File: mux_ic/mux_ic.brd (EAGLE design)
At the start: 160 x 100 mm, 12 parts, among them U2 TEXAS_INSTRUMENTS_CD74HC4067M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, U5 TEXAS_INSTRUMENTS_CD74HC4067M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, U6 TEXAS_INSTRUMENTS_CD74HC4067M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, U7 TEXAS_INSTRUMENTS_CD74HC4067M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

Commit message: update
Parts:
- moved U7 21.8 mm to (40.6, 66.0)
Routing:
- net N$22: track 0.00 -> 9.84 mm
- net N$21: track 0.00 -> 6.34 mm

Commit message: update to receive and send
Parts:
- moved JP4 33.3 mm to (64.8, 5.08)
- moved U7 22.9 mm to (40.6, 43.2)
- moved JP5 17.7 mm to (50.8, 5.08)
- moved JP3 16.9 mm to (12.7, 19.1)
- moved JP6 15.5 mm to (36.8, 5.08)
- moved JP8 14.5 mm to (73.7, 20.3), turned to 90 degrees
- moved U6 11.4 mm to (58.4, 43.2)
- moved JP2 10.9 mm to (2.54, 3.81)
- moved JP1 9.67 mm to (15.2, 30.5)
- moved JP7 8.89 mm to (22.9, 5.08)
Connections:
- removed net N$10: JP3.2, U7.1
- net N$4: now also JP3.2; no longer JP2.1
- net N$5: now also JP2.1, U7.1; no longer JP2.2
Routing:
- net N$21: track 6.34 -> 35.9 mm
- net N$22: track 9.84 -> 27.7 mm
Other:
- board size 160 x 100 mm -> 77.5 x 55.5 mm

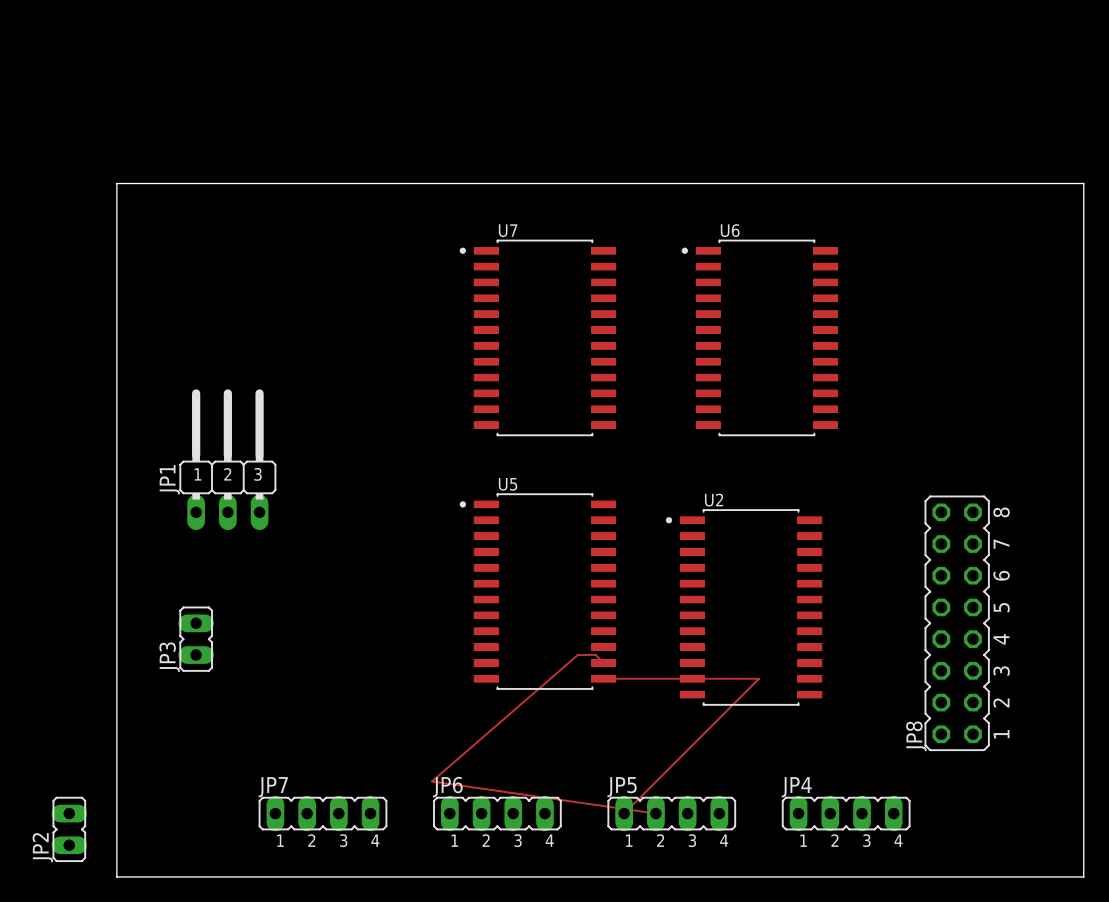
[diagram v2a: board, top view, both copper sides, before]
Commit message: Gentrified board layout and component names
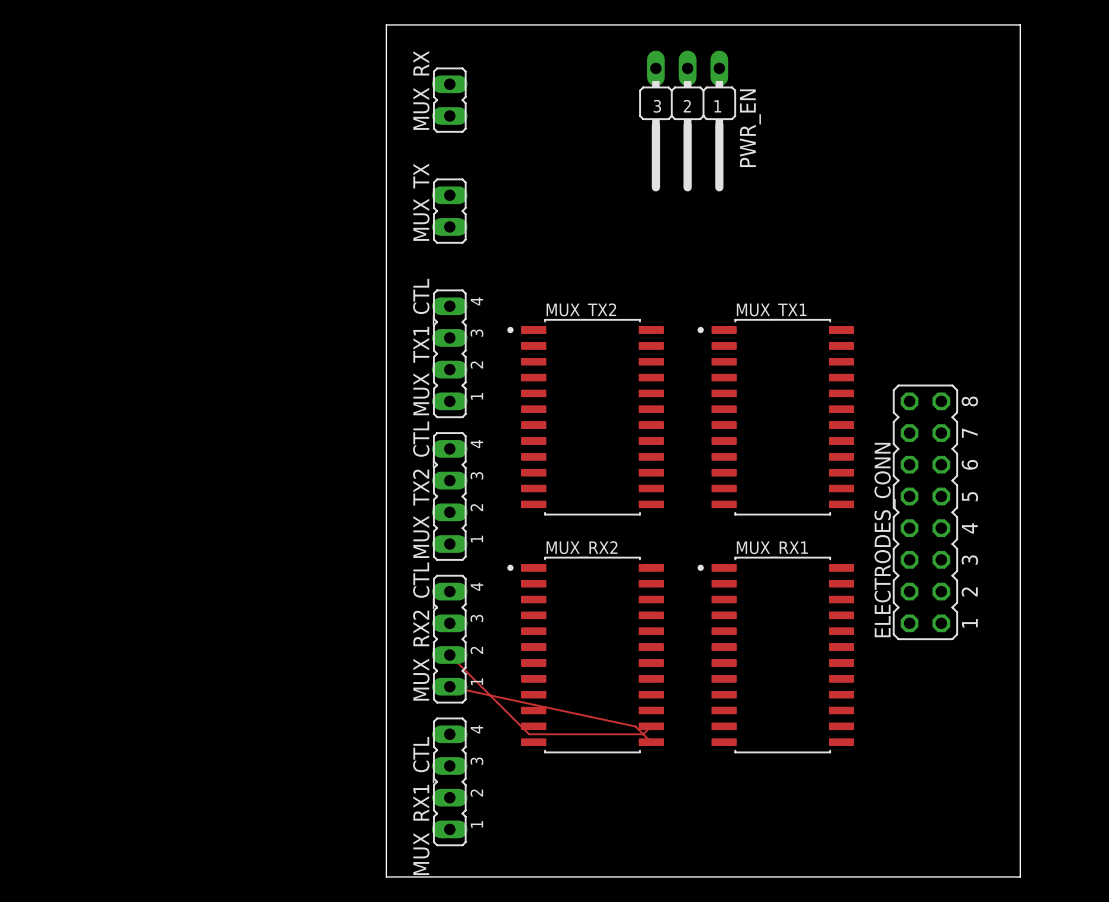
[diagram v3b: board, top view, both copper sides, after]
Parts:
- removed JP1: (no value), jumper:JP2W
- removed JP2, JP3: (no value), jumper:JP1
- removed JP4, JP5, JP6, JP7: (no value), jumper:JP4
- removed JP8: (no value), jumper:JP8Q
- removed U2, U5, U6, U7: TEXAS_INSTRUMENTS_CD74HC4067M96TEXAS_INSTRUMENTS_CD74HC4067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, Texas Instruments - CD74HC4067M96:TEXAS_INSTRUMENTS_CD74HC4067M96_0
- added ELECTRODES_CONN: (no value), jumper:JP8Q
- added MUX_RX, MUX_TX: (no value), jumper:JP1
- added MUX_RX1, MUX_RX2, MUX_TX1, MUX_TX2: TEXAS_INSTRUMENTS_CD74HC4067M96TEXAS_INSTRUMENTS_CD74HC4067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, Texas Instruments - CD74HC4067M96:TEXAS_INSTRUMENTS_CD74HC4067M96_0
- added MUX_RX1_CTL, MUX_RX2_CTL, MUX_TX1_CTL, MUX_TX2_CTL: (no value), jumper:JP4
- added PWR_EN: (no value), jumper:JP2W
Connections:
- removed net N$7: JP1.1, U2.15, U5.15, U6.15, U7.15
- removed net N$8: JP1.2, U2.24, U5.24, U6.24, U7.24
- removed net N$9: JP1.3, U2.12, U5.12, U6.12, U7.12
- new net EN: MUX_RX1.15, MUX_RX2.15, MUX_TX1.15, MUX_TX2.15, PWR_EN.1
- new net GND: MUX_RX1.12, MUX_RX2.12, MUX_TX1.12, MUX_TX2.12, PWR_EN.3
- new net N.C: MUX_TX.2
- new net VCC: MUX_RX1.24, MUX_RX2.24, MUX_TX1.24, MUX_TX2.24, PWR_EN.2
- net N$1: now also ELECTRODES_CONN.2, MUX_RX1.9, MUX_RX2.9, MUX_TX1.9, MUX_TX2.9; no longer JP8.2, U2.9, U5.9, U6.9, U7.9
- net N$11: now also MUX_TX1.10, MUX_TX1_CTL.4; no longer JP7.4, U6.10
- net N$12: now also MUX_TX1.11, MUX_TX1_CTL.3; no longer JP7.3, U6.11
- net N$13: now also MUX_TX1.14, MUX_TX1_CTL.2; no longer JP7.2, U6.14
- net N$14: now also MUX_TX1.13, MUX_TX1_CTL.1; no longer JP7.1, U6.13
- net N$15: now also MUX_TX2.13, MUX_TX2_CTL.1; no longer JP6.1, U7.13
- net N$16: now also MUX_TX2.14, MUX_TX2_CTL.2; no longer JP6.2, U7.14
- net N$17: now also MUX_TX2.11, MUX_TX2_CTL.3; no longer JP6.3, U7.11
- net N$18: now also MUX_TX2.10, MUX_TX2_CTL.4; no longer JP6.4, U7.10
- net N$19: now also MUX_RX2.10, MUX_RX2_CTL.4; no longer JP5.4, U5.10
- net N$2: now also ELECTRODES_CONN.1, ELECTRODES_CONN.10, ELECTRODES_CONN.12, ELECTRODES_CONN.13, ELECTRODES_CONN.14, ELECTRODES_CONN.15, ELECTRODES_CONN.16, ELECTRODES_CONN.3, ELECTRODES_CONN.4, ELECTRODES_CONN.5, ELECTRODES_CONN.6, ELECTRODES_CONN.7, ELECTRODES_CONN.8, ELECTRODES_CONN.9, MUX_RX1.16, MUX_RX1.17, MUX_RX1.18, MUX_RX1.19, MUX_RX1.2, MUX_RX1.20, MUX_RX1.22, MUX_RX1.23, MUX_RX1.3, MUX_RX1.4, MUX_RX1.5, MUX_RX1.6, MUX_RX1.7, MUX_RX1.8, MUX_RX2.16, MUX_RX2.17, MUX_RX2.18, MUX_RX2.19, MUX_RX2.2, MUX_RX2.20, MUX_RX2.22, MUX_RX2.23, MUX_RX2.3, MUX_RX2.4, MUX_RX2.5, MUX_RX2.6, MUX_RX2.7, MUX_RX2.8, MUX_TX1.16, MUX_TX1.17, MUX_TX1.18, MUX_TX1.19, MUX_TX1.2, MUX_TX1.20, MUX_TX1.22, MUX_TX1.23, MUX_TX1.3, MUX_TX1.4, MUX_TX1.5, MUX_TX1.6, MUX_TX1.7, MUX_TX1.8, MUX_TX2.16, MUX_TX2.17, MUX_TX2.18, MUX_TX2.19, MUX_TX2.2, MUX_TX2.20, MUX_TX2.22, MUX_TX2.23, MUX_TX2.3, MUX_TX2.4, MUX_TX2.5, MUX_TX2.6, MUX_TX2.7, MUX_TX2.8; no longer JP8.1, JP8.10, JP8.12, JP8.13, JP8.14, JP8.15, JP8.16, JP8.3, JP8.4, JP8.5, JP8.6, JP8.7, JP8.8, JP8.9, U2.16, U2.17, U2.18, U2.19, U2.2, U2.20, U2.22, U2.23, U2.3, U2.4, U2.5, U2.6, U2.7, U2.8, U5.16, U5.17, U5.18, U5.19, U5.2, U5.20, U5.22, U5.23, U5.3, U5.4, U5.5, U5.6, U5.7, U5.8, U6.16, U6.17, U6.18, U6.19, U6.2, U6.20, U6.22, U6.23, U6.3, U6.4, U6.5, U6.6, U6.7, U6.8, U7.16, U7.17, U7.18, U7.19, U7.2, U7.20, U7.22, U7.23, U7.3, U7.4, U7.5, U7.6, U7.7, U7.8
- net N$20: now also MUX_RX2.11, MUX_RX2_CTL.3; no longer JP5.3, U5.11
- net N$21: now also MUX_RX2.14, MUX_RX2_CTL.2; no longer JP5.2, U5.14
- net N$22: now also MUX_RX2.13, MUX_RX2_CTL.1; no longer JP5.1, U5.13
- net N$23: now also MUX_RX1.10, MUX_RX1_CTL.4; no longer JP4.4, U2.10
- net N$24: now also MUX_RX1.11, MUX_RX1_CTL.3; no longer JP4.3, U2.11
- net N$25: now also MUX_RX1.14, MUX_RX1_CTL.2; no longer JP4.2, U2.14
- net N$26: now also MUX_RX1.13, MUX_RX1_CTL.1; no longer JP4.1, U2.13
- net N$3: now also MUX_RX.1, MUX_RX1.1; no longer JP3.1, U2.1
- net N$4: now also MUX_RX.2, MUX_RX2.1; no longer JP3.2, U5.1
- net N$5: now also MUX_TX.1, MUX_TX1.1, MUX_TX2.1; no longer JP2.1, U6.1, U7.1
- net N$6: now also ELECTRODES_CONN.11, MUX_RX1.21, MUX_RX2.21, MUX_TX1.21, MUX_TX2.21; no longer JP8.11, U2.21, U5.21, U6.21, U7.21
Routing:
- net N$21: track 35.9 -> 19.0 mm
- net N$22: track 27.7 -> 17.0 mm
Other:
- board size 77.5 x 55.5 mm -> 50.8 x 68.2 mm

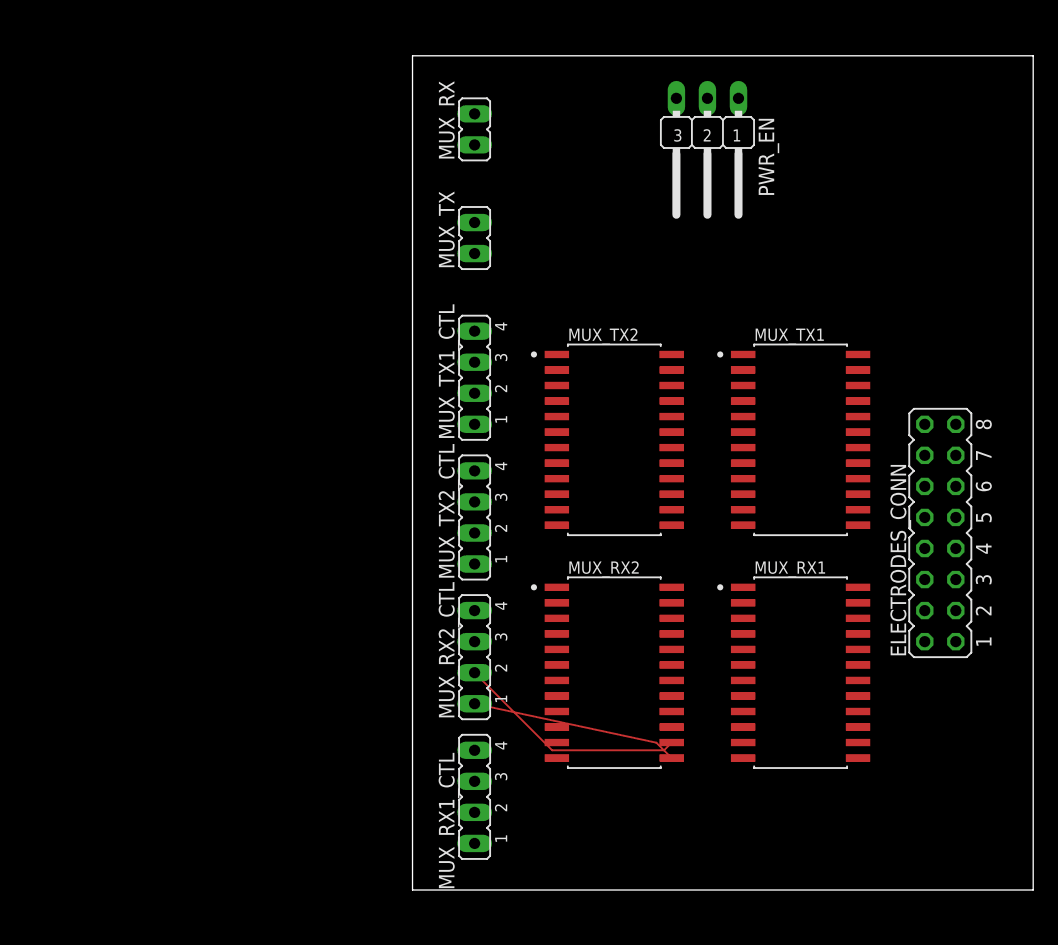
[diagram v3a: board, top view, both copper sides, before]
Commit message: Routed EarlyByrd board
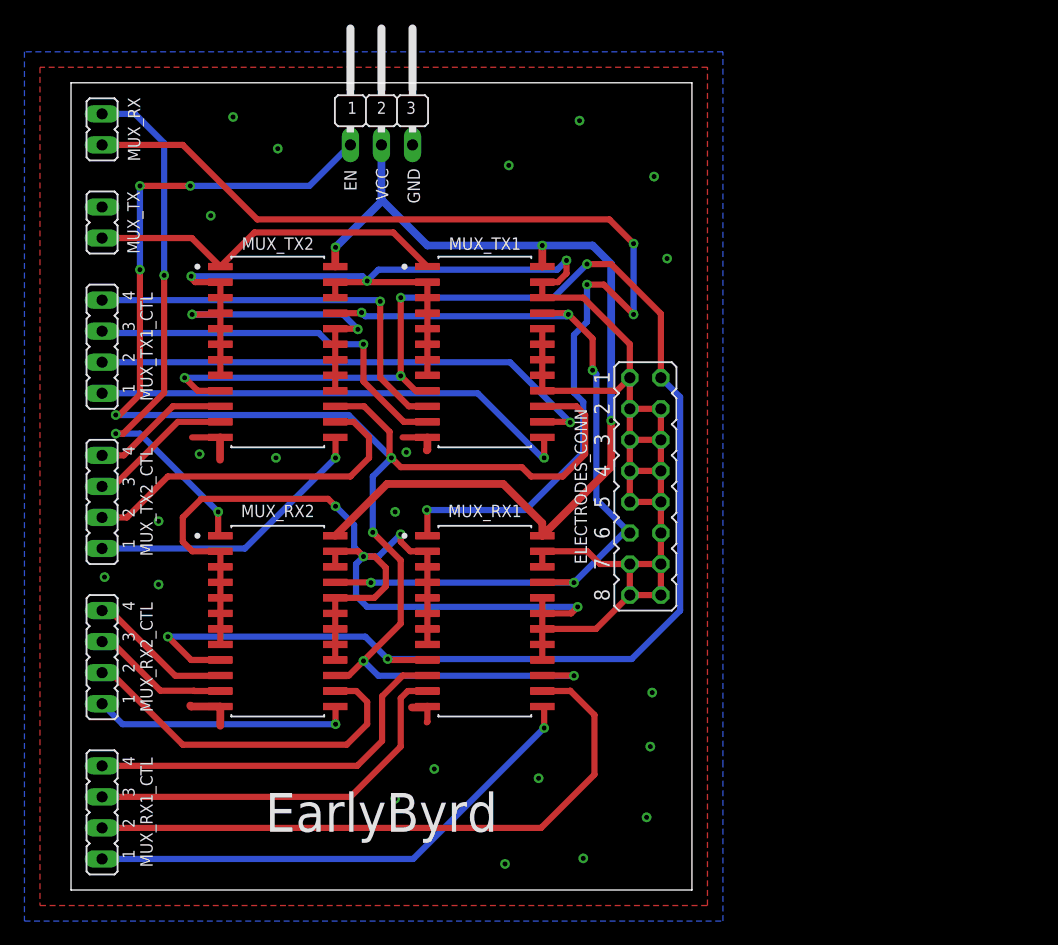
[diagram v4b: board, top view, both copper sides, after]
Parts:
- moved MUX_TX1_CTL 30.6 mm to (2.54, 44.5)
- moved MUX_RX1_CTL 30.5 mm to (2.54, 6.35)
- moved MUX_TX 30.5 mm to (2.54, 54.6)
- moved MUX_TX2_CTL 30.5 mm to (2.54, 31.8)
- moved MUX_RX 30.5 mm to (2.54, 62.2)
- moved MUX_RX2_CTL 30.5 mm to (2.54, 19.1)
- moved MUX_TX2 28.5 mm to (16.9, 44.0)
- moved MUX_RX2 27.9 mm to (16.9, 22.0)
- moved MUX_TX1 26.8 mm to (33.9, 44.0)
- moved PWR_EN 26.7 mm to (25.4, 62.2), turned to 0 degrees
- moved MUX_RX1 26.2 mm to (33.9, 22.0)
- moved ELECTRODES_CONN 24.4 mm to (47.0, 33.0), turned to 270 degrees
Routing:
- net N$2: track 0.00 -> 264.2 mm, vias 0 -> 9
- net EN: track 0.00 -> 136.7 mm, vias 0 -> 8
- net N$1: track 0.00 -> 131.9 mm, vias 0 -> 6
- net N$3: track 0.00 -> 88.8 mm, vias 0 -> 4
- net VCC: track 0.00 -> 79.8 mm, vias 0 -> 3
- net N$6: track 0.00 -> 69.8 mm, vias 0 -> 5
- net N$25: track 0.00 -> 52.1 mm
- net N$4: track 0.00 -> 44.9 mm, vias 0 -> 3
- net N$13: track 0.00 -> 42.7 mm, vias 0 -> 1
- net N$26: track 0.00 -> 42.4 mm, vias 0 -> 1
- net N$14: track 0.00 -> 40.1 mm, vias 0 -> 1
- net N$11: track 0.00 -> 33.9 mm, vias 0 -> 1
- net N$24: track 0.00 -> 32.5 mm
- net N$23: track 0.00 -> 31.8 mm
- net N$12: track 0.00 -> 31.5 mm, vias 0 -> 1
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- added copper zone on layer 1, net GND
- added copper zone on layer 16, net GND
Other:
- board size 50.8 x 68.2 mm -> 50.8 x 66 mm
- board text added: "EN"
- board text added: "EarlyByrd"
- board text added: "GND"
- board text added: "VCC"
